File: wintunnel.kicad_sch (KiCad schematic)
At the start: 16 parts, among them J3 wind tunnel side, J4 Control module side, M1 Stepper_Motor_bipolar, SW1 AC Switch, U1 BMP280, U2 MPXV7002DP, U3 AS5600

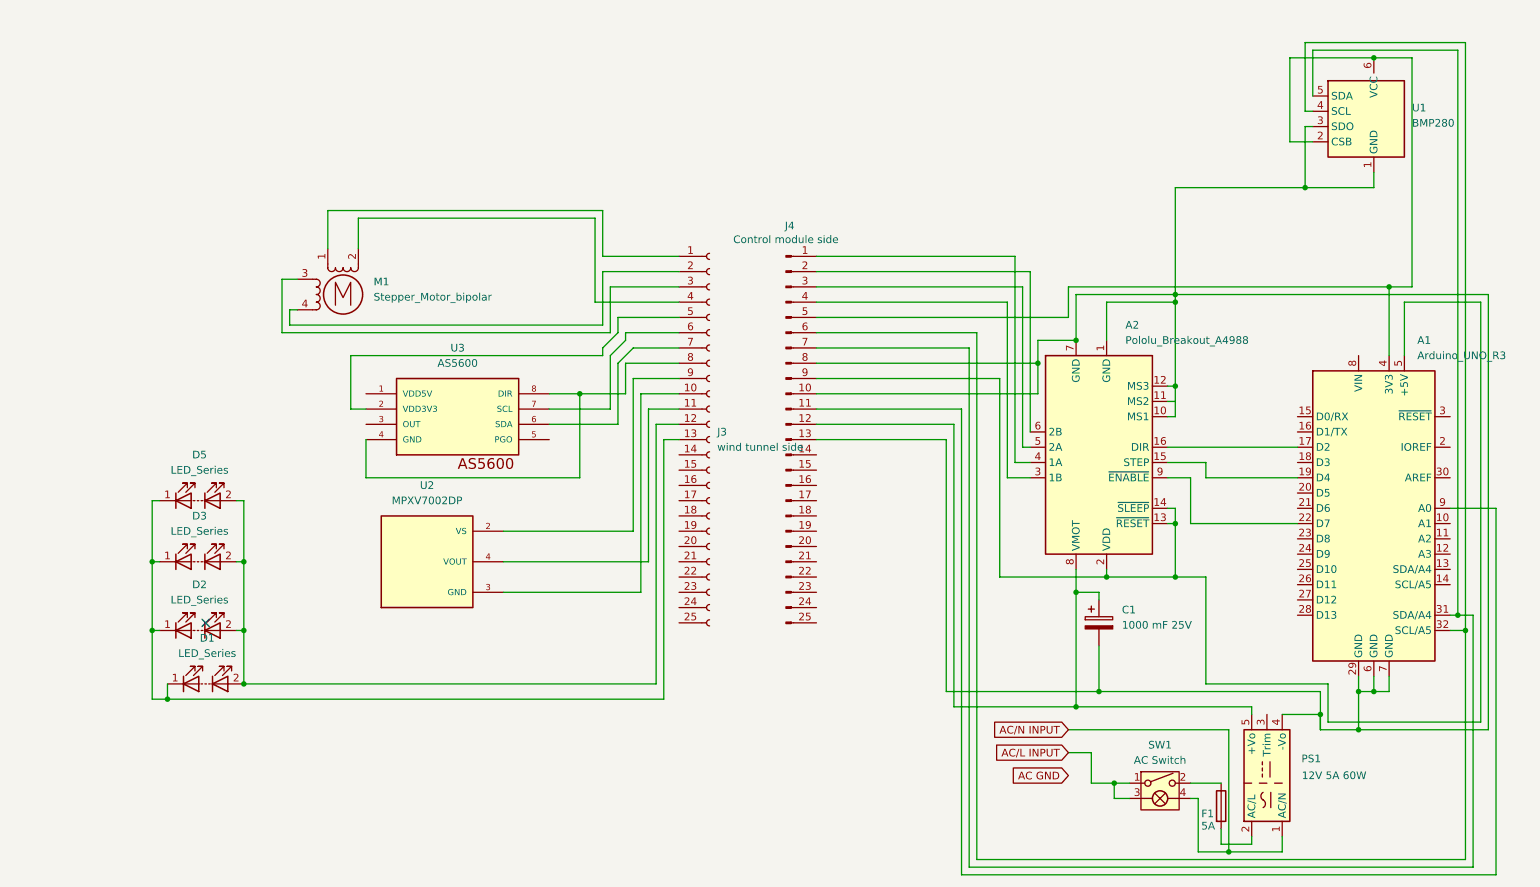
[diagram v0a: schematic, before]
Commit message: Added elements for pwm control of led lights via potentiometer
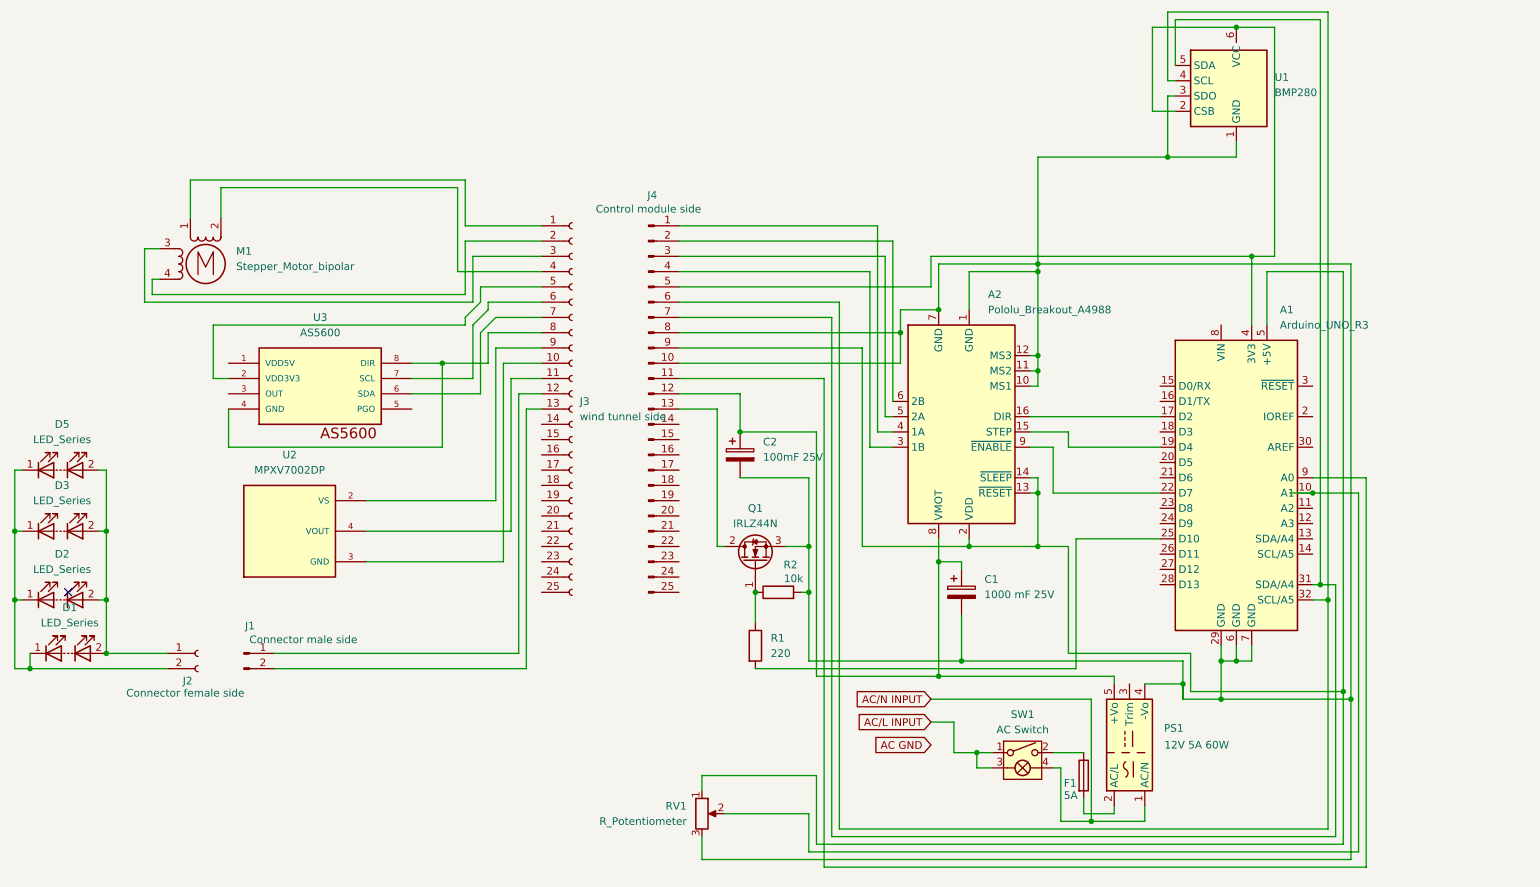
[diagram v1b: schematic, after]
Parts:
- added C2: 100mF 25V, symbol Device:C_Polarized
- added J1: Connector male side, symbol Connector:Conn_01x02_Pin
- added J2: Connector female side, symbol Connector:Conn_01x02_Socket
- added Q1: IRLZ44N, Package_TO_SOT_THT:TO-220-3_Vertical, symbol Transistor_FET:IRLZ44N
- added R1: 220, symbol Device:R
- added R2: 10k, symbol Device:R
- added RV1: R_Potentiometer, symbol Device:R_Potentiometer
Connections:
- net at A1.29 (GND), A1.6 (GND), A1.7 (GND)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: now also A2.11 (MS2), C2.2, Q1.3 (S), R2.2, RV1.3; no longer J4.13 (Pin_13)
- net at A2.8 (VMOT), C1.1, J4.12 (Pin_12)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: now also C2.1
- net at A1.5 (+5V), A2.13 (~{RESET}), A2.14 (~{SLEEP})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: now also RV1.1
- net at D1.2 (A), D2.2 (A), D3.2 (A)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: now also J2.1 (Pin_1); no longer J3.12 (Pin_12)
- net at D1.1 (K), D2.1 (K), D3.1 (K)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: now also J2.2 (Pin_2); no longer J3.13 (Pin_13)
- net at A1.10 (A1): now also RV1.2
- net at A1.25 (D10): now also R1.2
- new net: J1.1 (Pin_1), J3.12 (Pin_12)
- new net: J1.2 (Pin_2), J3.13 (Pin_13)
- new net: J4.13 (Pin_13), Q1.2 (D)
- new net: Q1.1 (G), R1.1, R2.1
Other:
- moved on the sheet: A1, A2, C1, D1, D2, D3, D5, F1, J3, J4, M1, PS1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
